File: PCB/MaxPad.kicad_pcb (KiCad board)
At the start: 2 copper layers, 105 x 138 mm, 27 parts, among them J1 Conn_01x04_Pin, SW1 SW_Push, SW10 SW_Push, SW11 SW_Push, SW12 SW_Push, SW13 RotaryEncoder, SW2 SW_Push, SW3 SW_Push, SW4 SW_Push, SW5 SW_Push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

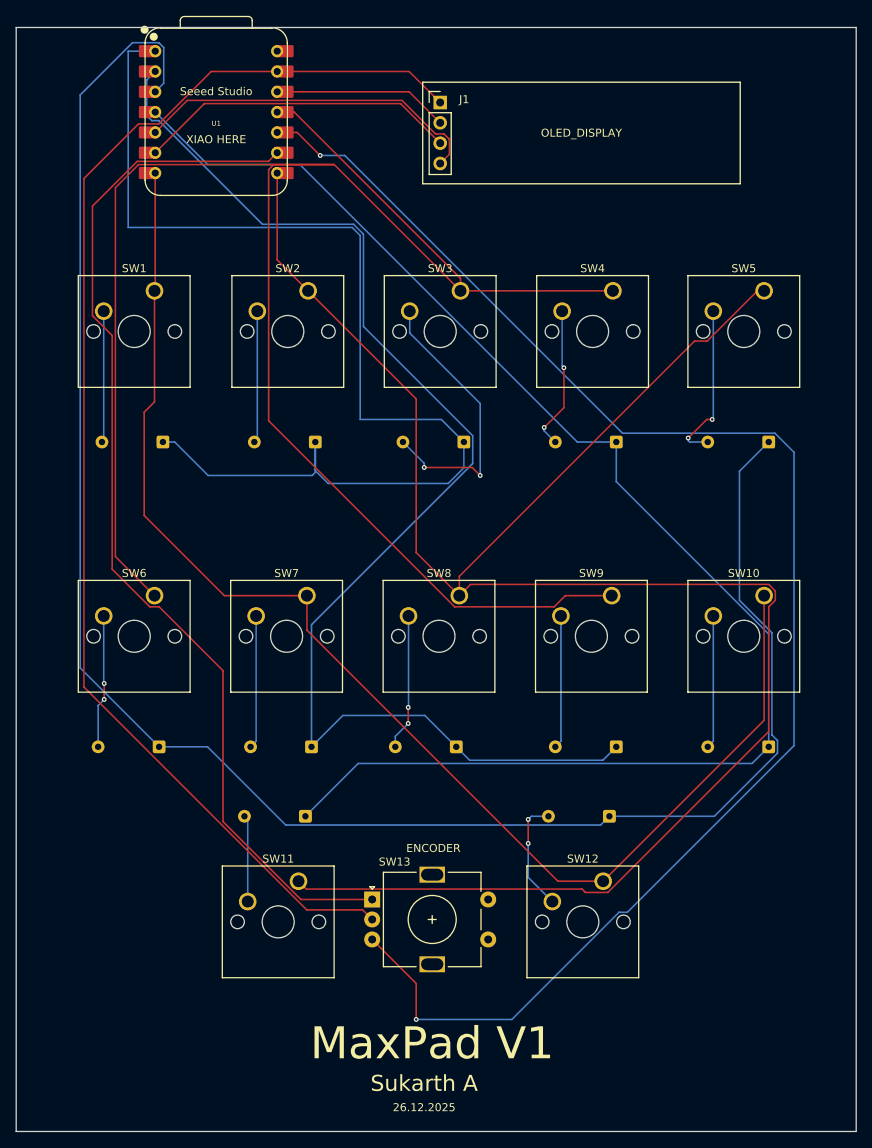
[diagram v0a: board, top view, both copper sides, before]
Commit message: Update to stay within max PCB size requirements
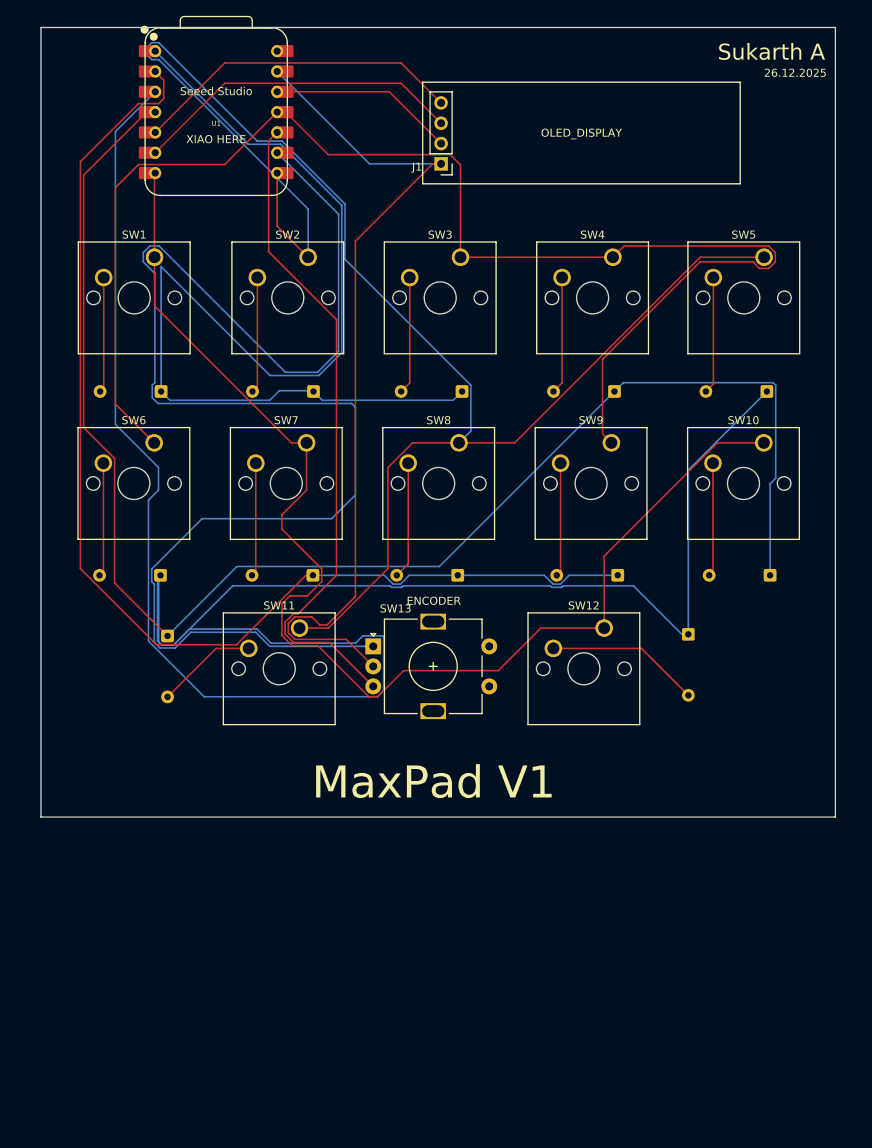
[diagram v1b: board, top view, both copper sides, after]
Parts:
- moved SW11 31.6 mm to (60.4, 97.1)
- moved SW12 31.6 mm to (98.5, 97.1)
- moved SW13 31.6 mm to (69.6, 99.4)
- moved D7 28.4 mm to (43.9, 98.1), turned to -90 degrees
- moved D9 24.8 mm to (109.0, 97.9), turned to -90 degrees
- moved D10 21.4 mm to (62.1, 90.5)
- moved D11 21.4 mm to (80.2, 90.5)
- moved D4 21.4 mm to (100.2, 90.5)
- moved D5 21.4 mm to (43.0, 90.5)
- moved D8 21.4 mm to (119.2, 90.5)
- moved SW10 19.1 mm to (118.5, 73.9)
- moved SW6 19.1 mm to (42.2, 73.9)
- moved SW7 19.1 mm to (61.3, 73.9)
- moved SW8 19.1 mm to (80.3, 73.9)
- moved SW9 19.1 mm to (99.4, 73.9)
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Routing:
- net Net-(U1-GPIO4/MISO): track 191.5 -> 83.4 mm, vias 2 -> 0
- net Net-(U1-GPIO3/MOSI): track 249.0 -> 174.9 mm
- net Net-(J1-Pin_1): track 163.3 -> 108.5 mm
- net Net-(U1-GPIO2/SCK): track 132.9 -> 183.9 mm
- net Net-(U1-GPIO1/RX): track 243.6 -> 202.2 mm
- net Net-(D12-K): track 232.4 -> 266.7 mm
- net Net-(D3-A): track 35.9 -> 14.7 mm, vias 2 -> 0
- net Net-(D10-K): track 160.0 -> 144.9 mm
- net Net-(U1-GPIO0/TX): track 166.2 -> 155.3 mm
- net Net-(D1-K): track 143.6 -> 134.3 mm
- net Net-(D12-A): track 20.4 -> 14.6 mm, vias 2 -> 0
- net Net-(D6-K): track 182.2 -> 187.5 mm
- net Net-(D9-A): track 14.2 -> 19.3 mm, vias 2 -> 0
- net Net-(D6-A): track 18.0 -> 14.7 mm, vias 2 -> 0
- net Net-(J1-Pin_4): track 43.9 -> 41.4 mm
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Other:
- board size 105 x 138 mm -> 99.3 x 98.7 mm
